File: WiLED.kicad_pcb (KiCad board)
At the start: 2 copper layers, 50 x 50 mm, 62 parts, among them J1 Mount, J2 Mount, J3 Mount, J4 Mount, P1 Serial to USB, P2 DC In, P4 LED Out, SW1 Reset, SW2 Boot, SW3 Toggle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

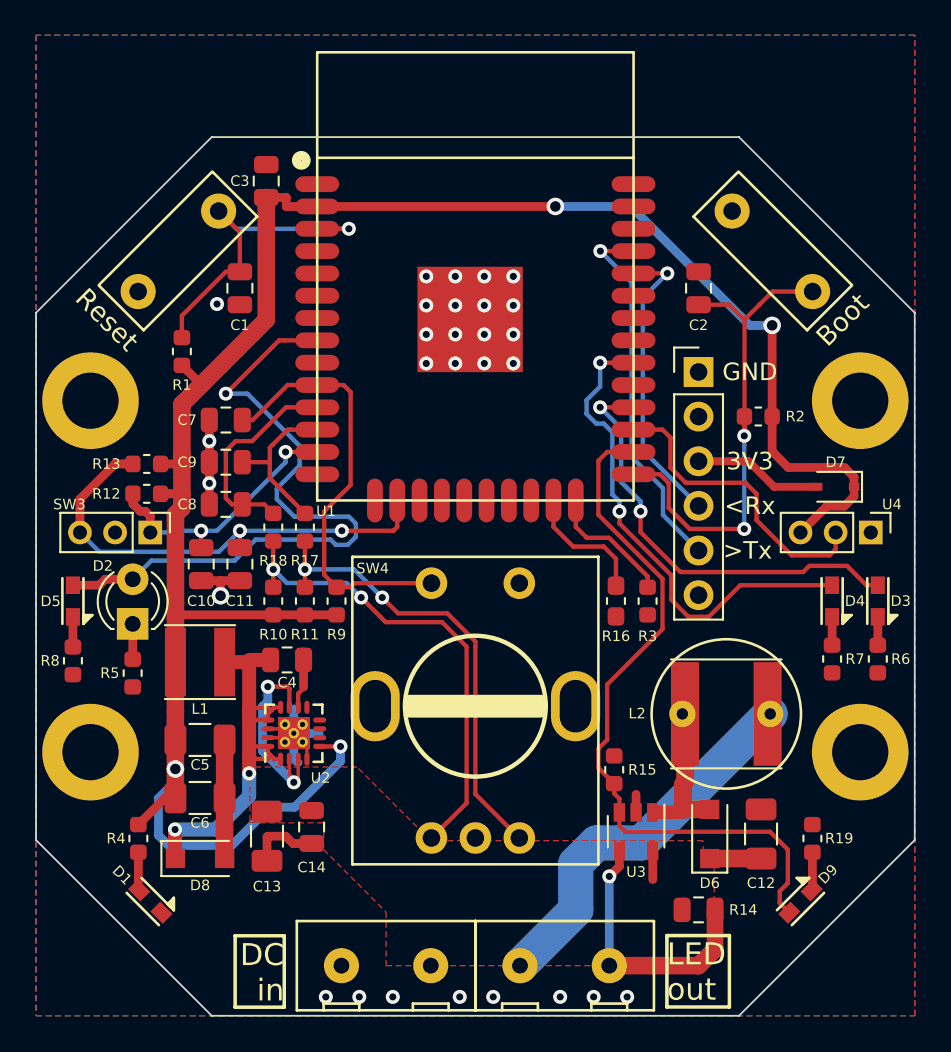
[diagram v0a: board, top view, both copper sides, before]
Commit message: Add stiching vias
Ground plane stitching vias have been added.
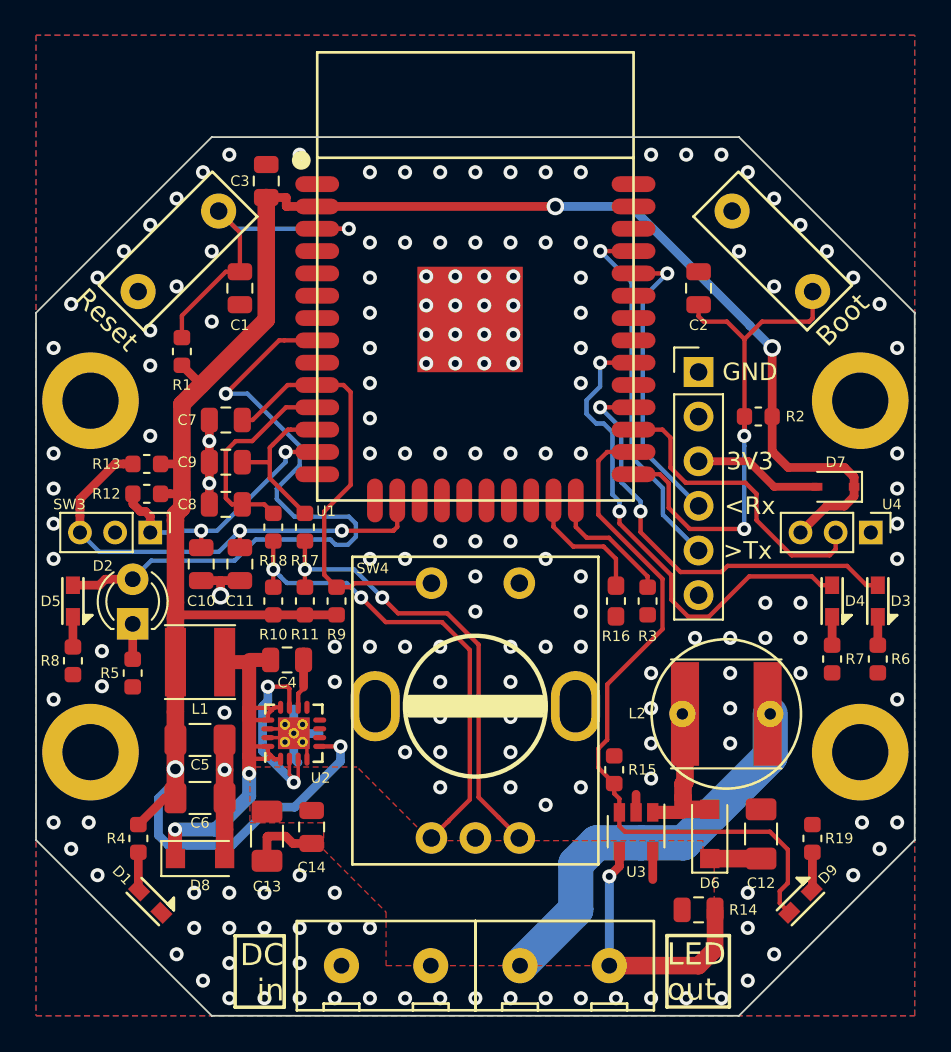
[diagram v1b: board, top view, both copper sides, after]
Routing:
- net LED_NEG: track 21.7 -> 23.1 mm
- net IO0: track 28.9 -> 29.9 mm
- net +3V3: track 120.2 -> 119.5 mm
- net GND: vias 28 -> 175

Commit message: Finalise v3.0 layout, add ESP32 3D model
Layout is now complete for the v3.0 board, pending a review. Stitching
vias are in place, and silkscreen has been updated.
Also added a 3D model for the ESP32, to help with modelling the
enclosure.
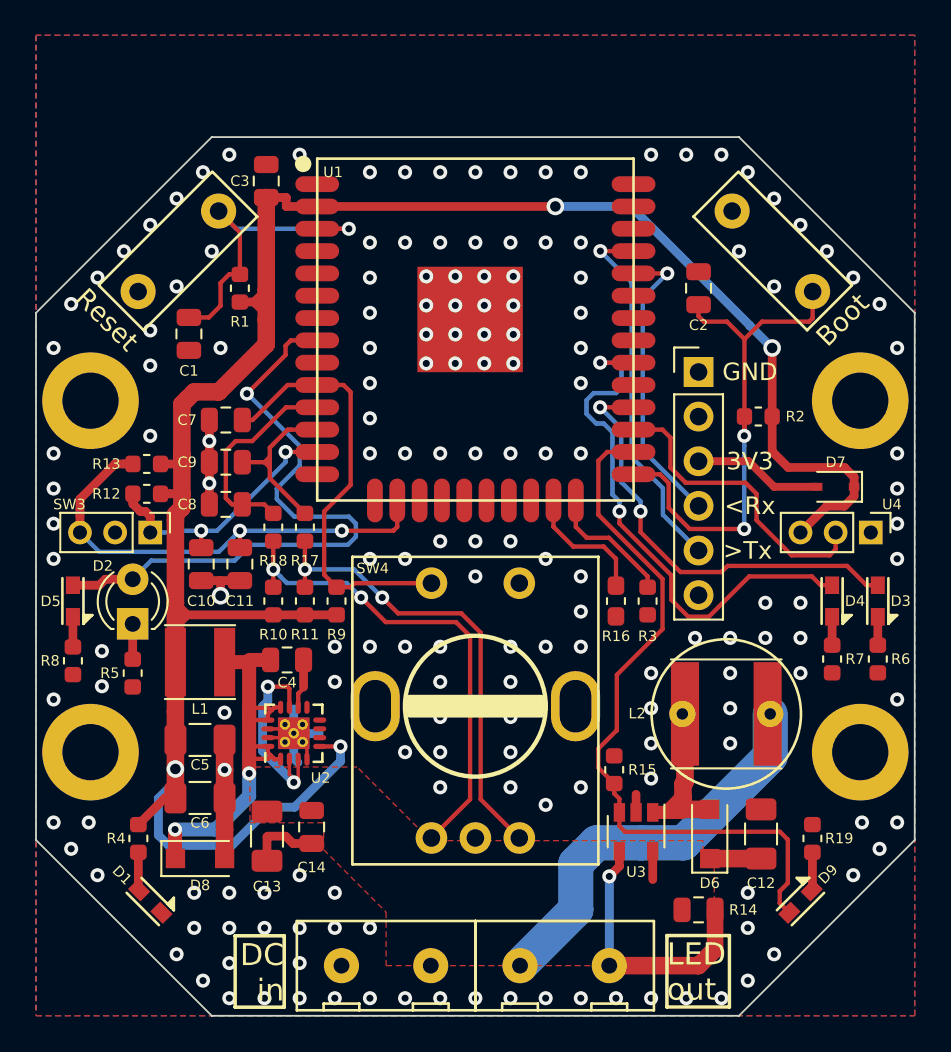
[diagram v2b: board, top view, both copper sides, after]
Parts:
- U1: footprint ESP32-footprints-Lib:ESP32-WROOM -> custom-footprints:ESP32-WROOM
- moved REF** 7.50 mm to (172.7, 95.0)
- moved R1 4.88 mm to (159.3, 86.2)
- moved C1 3.89 mm to (156.4, 88.8)
- moved REF** 2.20 mm to (172.7, 112.2)
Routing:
- net +3V3: track 119.5 -> 124.0 mm
- net IND_PWM: track 38.8 -> 36.4 mm
- net IO18: track 28.7 -> 31.0 mm
- net Net-(D6-Pad2): track 8.79 -> 10.1 mm
- net ENC_B: track 9.26 -> 10.1 mm
- net EN: track 19.2 -> 18.6 mm
- net GND: vias 175 -> 174
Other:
- board text added: "PIR"
- board text added: "Rx<"
- board text added: "Toggle"
- board text added: "Trigger"
- board text added: "Tx>"
- board text added: "UART"
- board text added: "https://wiled.tech/"
- board text removed: "https://git.io/WiLED-pcb"

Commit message: Update URL on silkscreen
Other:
- board text added: "https://wiled.cc/"
- board text removed: "https://wiled.tech/"
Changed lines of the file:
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@@
   (title_block
     (title "WiLED ESP32 Base")
-    (date 2018-09-23)
+    (date 2018-09-24)
     (rev 3.0)
     (comment 4 "Released under the CERN Open Hardware Licence v1.2")
@@
   )
   (gr_line (start 157.72 77.566) (end 187.72 77.566) (layer Edge.Cuts) (width 0.1))
-  (gr_text https://wiled.tech/ (at 172.72 105.366) (layer B.SilkS)
+  (gr_text https://wiled.cc/ (at 172.72 105.366) (layer B.SilkS)
     (effects (font (size 1.5 1.5) (thickness 0.2)) (justify mirror))
   )

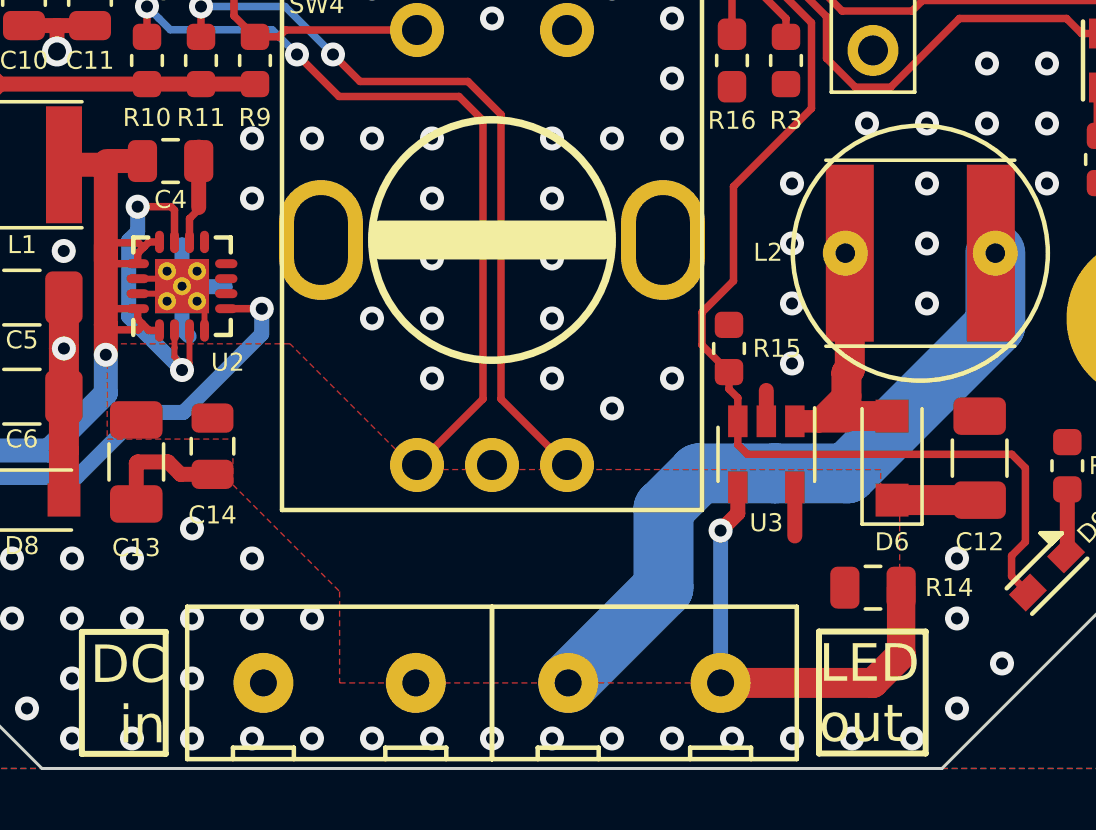
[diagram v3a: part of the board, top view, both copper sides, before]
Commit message: Update 3D models for terminal block and encoder
Found some manufacturer-supplied 3D models for the rotary encoder and
the terminal block, so added these to the PCB.
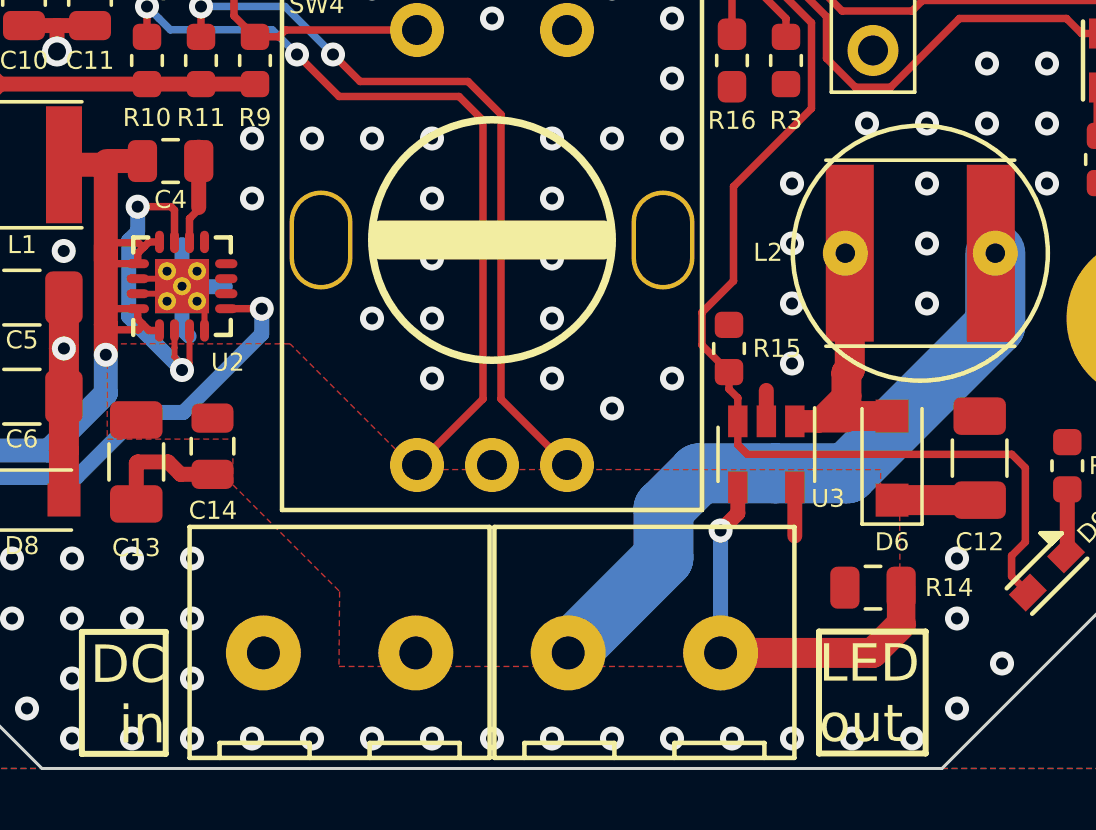
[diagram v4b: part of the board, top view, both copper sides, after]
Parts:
- moved P2 1.00 mm to (167.6, 123.7)
- moved P4 1.00 mm to (177.8, 123.7)
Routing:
- net LED_POS: track 15.4 -> 14.4 mm
- net LED_NEG: track 23.1 -> 22.1 mm
- net GND: vias 174 -> 171

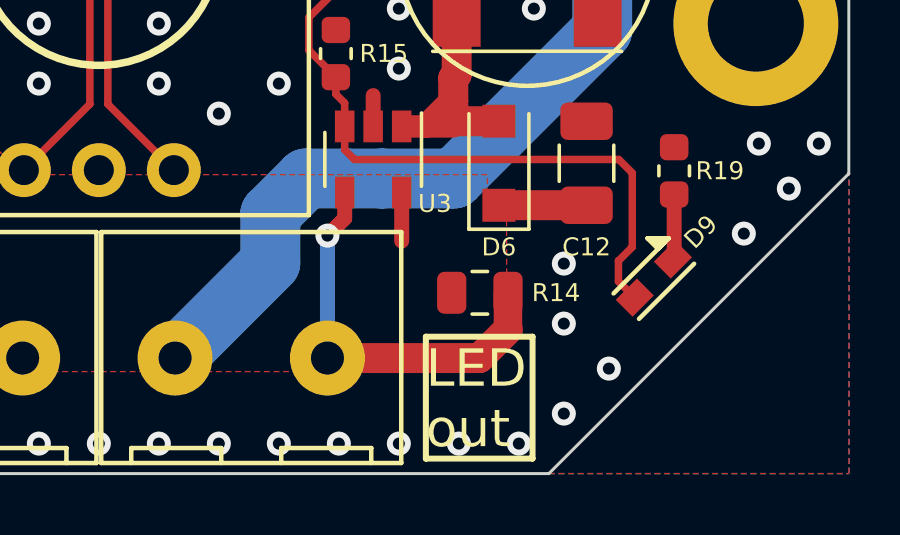
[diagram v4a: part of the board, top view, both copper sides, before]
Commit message: Change R14 to 0603 size
R14 was originally an 0603 in v1.0, but was changed to an 0805 - looking
at parts, 0603 are cheaper and still have the required values and
tolerances, so 0603 should be used instead.
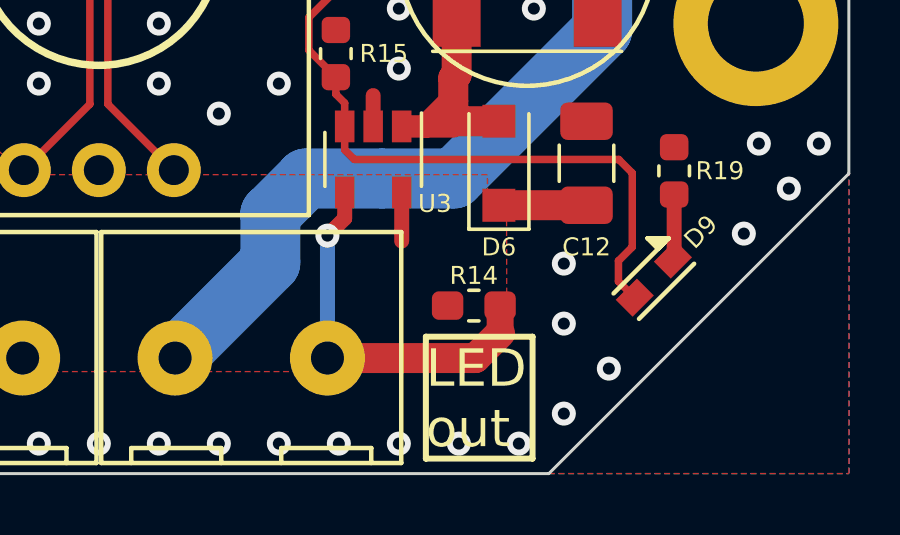
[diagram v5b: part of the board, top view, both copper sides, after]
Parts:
- R14: footprint Resistor_SMD:R_0805_2012Metric -> Resistor_SMD:R_0603_1608Metric_Pad1.05x0.95mm_HandSolder
- moved R14 0.47 mm to (185.2, 122.0)
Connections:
- SW4 pad : GND -> (no net)
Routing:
- net LED_POS: track 14.4 -> 13.8 mm
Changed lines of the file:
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@@
   (title_block
     (title "WiLED ESP32 Base")
-    (date 2018-09-25)
+    (date 2018-10-02)
     (rev 3.0)
     (comment 4 "Released under the CERN Open Hardware Licence v1.2")
@@
     (add_net RAW)
   )
+  (module Resistor_SMD:R_0603_1608Metric_Pad1.05x0.95mm_HandSolder (layer F.Cu)
+    (at 185.22 121.966 180)
+    (descr "Resistor SMD 0603 (1608 Metric), square (rectangular) end terminal, IPC_7351 nominal with elongated pad for handsoldering. (Body size source: http://www.tortai-tech.com/upload/download/2011102023233369053.pdf), generated with kicad-footprint-generator")
+    (tags "resistor handsolder")
+    (attr smd)
+    (fp_text reference R14 (at 0 1 180) (layer F.SilkS)
+      (effects (font (size 0.6 0.6) (thickness 0.12)))
+    )
+    (fp_text value 0.27 (at 0 1.43 180) (layer F.Fab) hide
+      (effects (font (size 1 1) (thickness 0.15)))
+    )
+    (fp_text user %R (at 0 0 180) (layer F.Fab)
+      (effects (font (size 0.4 0.4) (thickness 0.06)))
+    )
+    (fp_line (start 1.65 0.73) (end -1.65 0.73) (layer F.CrtYd) (width 0.05))
+    (fp_line (start 1.65 -0.73) (end 1.65 0.73) (layer F.CrtYd) (width 0.05))
+    (fp_line (start -1.65 -0.73) (end 1.65 -0.73) (layer F.CrtYd) (width 0.05))
+    (fp_line (start -1.65 0.73) (end -1.65 -0.73) (layer F.CrtYd) (width 0.05))
+    (fp_line (start -0.171267 0.51) (end 0.171267 0.51) (layer F.SilkS) (width 0.12))
+    (fp_line (start -0.171267 -0.51) (end 0.171267 -0.51) (layer F.SilkS) (width 0.12))
+    (fp_line (start 0.8 0.4) (end -0.8 0.4) (layer F.Fab) (width 0.1))
+    (fp_line (start 0.8 -0.4) (end 0.8 0.4) (layer F.Fab) (width 0.1))
+    (fp_line (start -0.8 -0.4) (end 0.8 -0.4) (layer F.Fab) (width 0.1))
+    (fp_line (start -0.8 0.4) (end -0.8 -0.4) (layer F.Fab) (width 0.1))
+    (pad 2 smd roundrect (at 0.875 0 180) (size 1.05 0.95) (layers F.Cu F.Paste F.Mask) (roundrect_rratio 0.25)
+      (net 5 RAW))
+    (pad 1 smd roundrect (at -0.875 0 180) (size 1.05 0.95) (layers F.Cu F.Paste F.Mask) (roundrect_rratio 0.25)
+      (net 21 LED_POS))
+    (model ${KISYS3DMOD}/Resistor_SMD.3dshapes/R_0603_1608Metric.wrl
+      (at (xyz 0 0 0))
+      (scale (xyz 1 1 1))
+      (rotate (xyz 0 0 0))
+    )
+  )
   (module custom-footprints:PEC11R_5 locked (layer F.Cu)
     (at 172.72 109.95)
@@
     (fp_line (start -3.75 0) (end 3.75 0) (layer F.SilkS) (width 0.5))
     (fp_circle (center 0 0) (end 4 0.25) (layer F.SilkS) (width 0.25))
-    (pad "" thru_hole oval (at -5.7 0) (size 2.1 3.3) (drill oval 1.8 3) (layers *.Cu B.Mask)
-      (net 2 GND))
-    (pad "" thru_hole oval (at 5.7 0) (size 2.1 3.3) (drill oval 1.8 3) (layers *.Cu B.Mask)
-      (net 2 GND))
+    (pad "" thru_hole oval (at -5.7 0) (size 2.1 3.3) (drill oval 1.8 3) (layers *.Cu B.Mask))
+    (pad "" thru_hole oval (at 5.7 0) (size 2.1 3.3) (drill oval 1.8 3) (layers *.Cu B.Mask))
     (pad 4 thru_hole circle (at -2.5 -7) (size 1.8 1.8) (drill 1) (layers *.Cu *.Mask)
       (net 6 ENC_SW))
@@
     )
   )
-  (module Resistor_SMD:R_0805_2012Metric (layer F.Cu)
-    (at 185.42 121.539 180)
-    (descr "Resistor SMD 0805 (2012 Metric), square (rectangular) end terminal, IPC_7351 nominal, (Body size source: https://docs.google.com/spreadsheets/d/1BsfQQcO9C6DZCsRaXUlFlo91Tg2WpOkGARC1WS5S8t0/edit?usp=sharing), generated with kicad-footprint-generator")
-    (tags resistor)
-    (attr smd)
-    (fp_text reference R14 (at -2.54 0) (layer F.SilkS)
-      (effects (font (size 0.6 0.6) (thickness 0.12)))
-    )
-    (fp_text value 0.27 (at 0 1.65 180) (layer F.Fab) hide
-      (effects (font (size 1 1) (thickness 0.15)))
-    )
-    (fp_line (start -1 0.6) (end -1 -0.6) (layer F.Fab) (width 0.1))
-    (fp_line (start -1 -0.6) (end 1 -0.6) (layer F.Fab) (width 0.1))
-    (fp_line (start 1 -0.6) (end 1 0.6) (layer F.Fab) (width 0.1))
-    (fp_line (start 1 0.6) (end -1 0.6) (layer F.Fab) (width 0.1))
-    (fp_line (start -0.258578 -0.71) (end 0.258578 -0.71) (layer F.SilkS) (width 0.12))
-    (fp_line (start -0.258578 0.71) (end 0.258578 0.71) (layer F.SilkS) (width 0.12))
-    (fp_line (start -1.68 0.95) (end -1.68 -0.95) (layer F.CrtYd) (width 0.05))
-    (fp_line (start -1.68 -0.95) (end 1.68 -0.95) (layer F.CrtYd) (width 0.05))
-    (fp_line (start 1.68 -0.95) (end 1.68 0.95) (layer F.CrtYd) (width 0.05))
-    (fp_line (start 1.68 0.95) (end -1.68 0.95) (layer F.CrtYd) (width 0.05))
-    (fp_text user %R (at 0 0 180) (layer F.Fab)
-      (effects (font (size 0.5 0.5) (thickness 0.08)))
-    )
-    (pad 1 smd roundrect (at -0.9375 0 180) (size 0.975 1.4) (layers F.Cu F.Paste F.Mask) (roundrect_rratio 0.25)
-      (net 21 LED_POS))
-    (pad 2 smd roundrect (at 0.9375 0 180) (size 0.975 1.4) (layers F.Cu F.Paste F.Mask) (roundrect_rratio 0.25)
-      (net 5 RAW))
-    (model ${KISYS3DMOD}/Resistor_SMD.3dshapes/R_0805_2012Metric.wrl
-      (at (xyz 0 0 0))
-      (scale (xyz 1 1 1))
-      (rotate (xyz 0 0 0))
-    )
-  )
   (module Resistor_SMD:R_0603_1608Metric (layer F.Cu)
     (at 180.62 113.566 90)
@@
   (segment (start 180.914 118.194) (end 180.914 119.06) (width 0.5) (layer F.Cu) (net 21))
   (segment (start 180.34 119.634) (end 180.34 124.714) (width 0.5) (layer B.Cu) (net 21))
-  (segment (start 185.4095 123.714) (end 186.3575 122.766) (width 1) (layer F.Cu) (net 21))
-  (segment (start 180.34 123.714) (end 185.4095 123.714) (width 1) (layer F.Cu) (net 21))
-  (segment (start 186.3575 121.539) (end 186.3575 122.766) (width 0.95) (layer F.Cu) (net 21))
+  (segment (start 180.34 123.714) (end 185.272 123.714) (width 1) (layer F.Cu) (net 21))
+  (segment (start 186.095 122.891) (end 186.095 121.966) (width 0.9) (layer F.Cu) (net 21))
+  (segment (start 185.272 123.714) (end 186.095 122.891) (width 1) (layer F.Cu) (net 21))
   (segment (start 180.32 100.366) (end 182.52 102.566) (width 0.25) (layer F.Cu) (net 22))
   (segment (start 182.52 102.566) (end 182.52 103.1785) (width 0.25) (layer F.Cu) (net 22))

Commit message: Change C12 and C13 to through-hole electrolytic caps
C12 and C13 were initially MLCCs, but these are harder to obtain and are
more expensive than electrolytics - for this use case, the swap should
be acceptable.
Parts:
- C12, C13: footprint Capacitor_SMD:C_1206_3216Metric -> Capacitor_THT:CP_Radial_D5.0mm_P2.00mm
- moved R19 2.64 mm to (194.5, 117.8), turned to 225 degrees
- moved R4 2.64 mm to (150.9, 117.8), turned to 135 degrees
- moved C13 1.58 mm to (160.9, 115.8)
- moved C14 1.32 mm to (164.7, 116.8)
- moved C6 1.20 mm to (155.8, 115.2)
- moved D6 1.04 mm to (185.1, 116.8)
- moved D8 0.93 mm to (156.1, 118.6)
- moved C5 0.80 mm to (156.2, 111.9)
- moved C12 0.57 mm to (189.3, 116.8), turned to 0 degrees
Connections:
- SW4 pad : (no net) -> GND
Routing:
- net GND: track 29.4 -> 18.5 mm, vias 171 -> 166
- net +3V3: track 124.0 -> 130.2 mm
- net LED_PWM: track 41.0 -> 46.8 mm
- net RAW: track 15.7 -> 12.5 mm
- net Net-(D6-Pad2): track 10.1 -> 7.64 mm
- net Net-(D9-Pad1): track 2.18 -> 3.18 mm
- net Net-(D1-Pad2): track 2.18 -> 3.12 mm
